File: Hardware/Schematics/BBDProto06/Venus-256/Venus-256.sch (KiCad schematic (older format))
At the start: 2 parts

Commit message: Added the hierarchical sheets
Added the hierarchical sheets for Cell Master and Slave
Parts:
- removed U? (x2): ATSAME70Q21A-AN, Package_QFP:LQFP-144_20x20mm_P0.5mm, symbol MCU_Microchip_SAME:ATSAME70Q21A-AN
- added C? (x14): 100nF, symbol Device:C_Small
- added C?: 10uF, symbol Device:C_Small
- added C?: 10pF, symbol Device:C_Small
- added D?: LED_ARGB, symbol Device:LED_ARGB
- added J406: ARM JTAG, symbol Connector_Generic:Conn_02x10_Odd_Even
- added J?: ADVREF, symbol Connector_Generic:Conn_01x01
- added L200: L, symbol Device:L
- added R400, R401, R402, R403: 0R, symbol Device:R_Small
- added R?: 5.62K, symbol Device:R_Small
- added U1: ATSAME70Q21A-AN, Package_QFP:LQFP-144_20x20mm_P0.5mm, symbol MCU_Microchip_SAME:ATSAME70Q21A-AN
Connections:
- net labels added: AFE0_AD0, AFE0_AD1, DAC0, DAC1, GND, SPI0_MISO, SPI0_MOSI, SPI0_SPCK, SPI1_MISO, SPI1_MOSI, SPI1_NPCS0, SPI1_NPCS1, SPI1_NPCS2, SPI1_NPCS3, SPI1_SPCK, SWCLK, SWDIO, TARGET_RESET, TRACESWO, USBD+, USBD-, VCC_3V3, VCC_MCU_P3V3, VDDCORE
- wire segments 0 -> 189
- no-connect marks 0 -> 8
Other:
- note added: "SWCLK"
- note added: "SWDIO"
- note added: "TARGET_RESET"
- note added: "TRACESWO"

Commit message: Updated the Cell Master and Slave schematics
Updated the Cell Master and Slave schematics
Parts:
- removed C? (x14): 100nF, symbol Device:C_Small
- removed C?: 10uF, symbol Device:C_Small
- removed C?: 10pF, symbol Device:C_Small
- removed D?: LED_ARGB, symbol Device:LED_ARGB
- removed J406: ARM JTAG, symbol Connector_Generic:Conn_02x10_Odd_Even
- removed J?: ADVREF, symbol Connector_Generic:Conn_01x01
- removed L200: L, symbol Device:L
- removed R400, R401, R402, R403: 0R, symbol Device:R_Small
- removed R?: 5.62K, symbol Device:R_Small
- removed U1: ATSAME70Q21A-AN, Package_QFP:LQFP-144_20x20mm_P0.5mm, symbol MCU_Microchip_SAME:ATSAME70Q21A-AN
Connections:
- net labels removed: AFE0_AD0, AFE0_AD1, DAC0, DAC1, GND, SPI0_MISO, SPI0_MOSI, SPI0_SPCK, SPI1_MISO, SPI1_MOSI, SPI1_NPCS0, SPI1_NPCS1, SPI1_NPCS2, SPI1_NPCS3, SPI1_SPCK, SWCLK, SWDIO, TARGET_RESET, TRACESWO, USBD+, USBD-, VCC_3V3, VCC_MCU_P3V3, VDDCORE
- wire segments 189 -> 0
- no-connect marks 8 -> 0
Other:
- note removed: "SWCLK"
- note removed: "SWDIO"
- note removed: "TARGET_RESET"
- note removed: "TRACESWO"

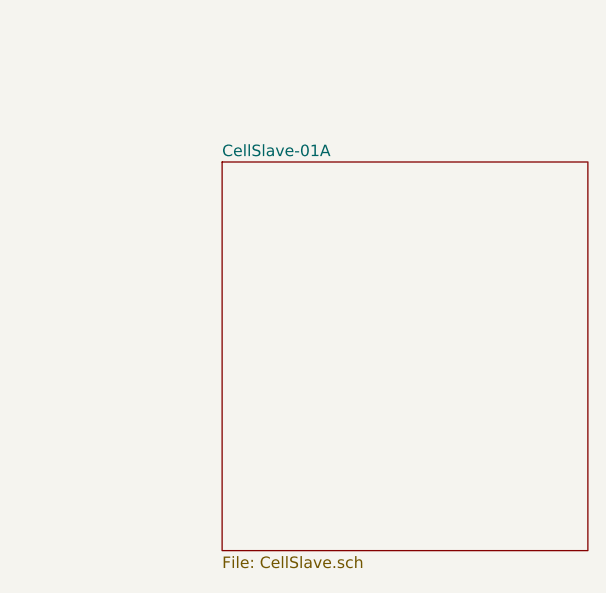
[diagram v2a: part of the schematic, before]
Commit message: Added Cell Slave capacitors
Added Cell Slave capacitors
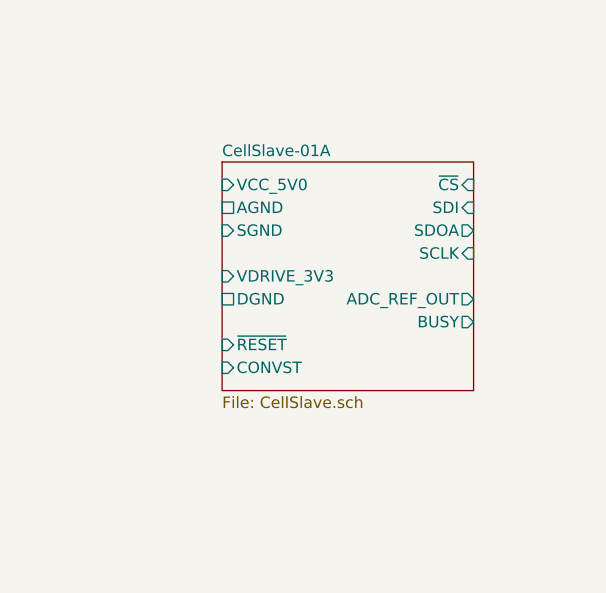
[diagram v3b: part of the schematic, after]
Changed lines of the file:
@@
 $EndSheet
 $Sheet
-S 5000 3500 1600 1700
+S 5000 3500 1100 1000
 U 5AE9ECEB
 F0 "CellSlave-01A" 50
 F1 "CellSlave.sch" 50
+F2 "DGND" U L 5000 4100 50
+F3 "BUSY" O R 6100 4200 50
+F4 "~CS" I R 6100 3600 50
+F5 "VDRIVE_3V3" I L 5000 4000 50
+F6 "SDI" I R 6100 3700 50
+F7 "SDOA" O R 6100 3800 50
+F8 "SCLK" I R 6100 3900 50
+F9 "AGND" U L 5000 3700 50
+F10 "VCC_5V0" I L 5000 3600 50
+F11 "SGND" I L 5000 3800 50
+F12 "ADC_REF_OUT" O R 6100 4100 50
+F13 "~RESET" I L 5000 4300 50
+F14 "CONVST" I L 5000 4400 50
 $EndSheet
 $EndSCHEMATC

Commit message: Completed the Cell Master and Slave schematics
Completed the Cell Master and Slave schematics
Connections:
- net labels added: GND
- wire segments 0 -> 148

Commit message: Added ADG715 switch array
Added ADG715 switch array
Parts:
- added U?: ADG715, Package_SO:TSSOP-24_4.4x7.8mm_P0.65mm, symbol Analog:ADG715
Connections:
- wire segments 148 -> 218

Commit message: Started to rearrange the Venus-256 PCB
Started to rearrange the Venus-256 PCB
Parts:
- gave numbers to parts that had none: 1
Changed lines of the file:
@@
 $Descr A4 11693 8268
 encoding utf-8
-Sheet 1 8
+Sheet 1 9
 Title "Venus-256"
 Date "2018-04-06"
@@
 $EndSheet
 $Comp
-L power:GND #PWR?
+L power:GND #PWR07
 U 1 1 5AE8F6FC
 P 4100 3300
-F 0 "#PWR?" H 4100 3050 50  0001 C CNN
+F 0 "#PWR07" H 4100 3050 50  0001 C CNN
 F 1 "GND" H 4105 3127 50  0000 C CNN
 F 2 "" H 4100 3300 50  0001 C CNN
@@
 	4100 3100 4100 3300
 $Comp
-L power:GND #PWR?
+L power:GND #PWR02
 U 1 1 5AE8F71C
 P 1000 3000
-F 0 "#PWR?" H 1000 2750 50  0001 C CNN
+F 0 "#PWR02" H 1000 2750 50  0001 C CNN
 F 1 "GND" H 1005 2827 50  0000 C CNN
 F 2 "" H 1000 3000 50  0001 C CNN
@@
 	1000 2800 1000 3000
 $Comp
-L power:GND #PWR?
+L power:GND #PWR01
 U 1 1 5AE8F730
 P 1000 1500
-F 0 "#PWR?" H 1000 1250 50  0001 C CNN
+F 0 "#PWR01" H 1000 1250 50  0001 C CNN
 F 1 "GND" H 1005 1327 50  0000 C CNN
 F 2 "" H 1000 1500 50  0001 C CNN
@@
 Connection ~ 800  1000
 $Comp
-L power:GND #PWR?
+L power:GND #PWR09
 U 1 1 5AE90A11
 P 9900 1600
-F 0 "#PWR?" H 9900 1350 50  0001 C CNN
+F 0 "#PWR09" H 9900 1350 50  0001 C CNN
 F 1 "GND" H 9905 1427 50  0000 C CNN
 F 2 "" H 9900 1600 50  0001 C CNN
@@
 	9900 1400 9900 1600
 $Comp
-L power:GND #PWR?
+L power:GND #PWR013
 U 1 1 5AE919C7
 P 10100 1600
-F 0 "#PWR?" H 10100 1350 50  0001 C CNN
+F 0 "#PWR013" H 10100 1350 50  0001 C CNN
 F 1 "GND" H 10105 1427 50  0000 C CNN
 F 2 "" H 10100 1600 50  0001 C CNN
@@
 	10400 2300 9800 2300
 $Comp
-L power:GND #PWR?
+L power:GND #PWR010
 U 1 1 5AE958F1
 P 9900 2900
-F 0 "#PWR?" H 9900 2650 50  0001 C CNN
+F 0 "#PWR010" H 9900 2650 50  0001 C CNN
 F 1 "GND" H 9905 2727 50  0000 C CNN
 F 2 "" H 9900 2900 50  0001 C CNN
@@
 	9900 2700 9900 2900
 $Comp
-L power:GND #PWR?
+L power:GND #PWR014
 U 1 1 5AE958F9
 P 10100 2900
-F 0 "#PWR?" H 10100 2650 50  0001 C CNN
+F 0 "#PWR014" H 10100 2650 50  0001 C CNN
 F 1 "GND" H 10105 2727 50  0000 C CNN
 F 2 "" H 10100 2900 50  0001 C CNN
@@
 	10400 3600 9800 3600
 $Comp
-L power:GND #PWR?
+L power:GND #PWR011
 U 1 1 5AE96319
 P 9900 4200
-F 0 "#PWR?" H 9900 3950 50  0001 C CNN
+F 0 "#PWR011" H 9900 3950 50  0001 C CNN
 F 1 "GND" H 9905 4027 50  0000 C CNN
 F 2 "" H 9900 4200 50  0001 C CNN
@@
 	9900 4000 9900 4200
 $Comp
-L power:GND #PWR?
+L power:GND #PWR015
 U 1 1 5AE96321
 P 10100 4200
-F 0 "#PWR?" H 10100 3950 50  0001 C CNN
+F 0 "#PWR015" H 10100 3950 50  0001 C CNN
 F 1 "GND" H 10105 4027 50  0000 C CNN
 F 2 "" H 10100 4200 50  0001 C CNN
@@
 	10400 4900 9800 4900
 $Comp
-L power:GND #PWR?
+L power:GND #PWR012
 U 1 1 5AE96EDB
 P 9900 5500
-F 0 "#PWR?" H 9900 5250 50  0001 C CNN
+F 0 "#PWR012" H 9900 5250 50  0001 C CNN
 F 1 "GND" H 9905 5327 50  0000 C CNN
 F 2 "" H 9900 5500 50  0001 C CNN
@@
 	9900 5300 9900 5500
 $Comp
-L power:GND #PWR?
+L power:GND #PWR016
 U 1 1 5AE96EE3
 P 10100 5500
-F 0 "#PWR?" H 10100 5250 50  0001 C CNN
+F 0 "#PWR016" H 10100 5250 50  0001 C CNN
 F 1 "GND" H 10105 5327 50  0000 C CNN
 F 2 "" H 10100 5500 50  0001 C CNN
@@
 	2800 1300 3500 1300
 $Comp
-L Analog:ADG715 U?
+L Analog:ADG715 U1
 U 1 1 5AE36C1A
 P 1800 4600
-F 0 "U?" H 1300 5200 50  0000 C CNN
+F 0 "U1" H 1300 5200 50  0000 C CNN
 F 1 "ADG715" H 1400 4100 50  0000 C CNN
 F 2 "Package_SO:TSSOP-24_4.4x7.8mm_P0.65mm" H 2800 4100 50  0001 C CIN
@@
 $EndComp
 $Comp
-L power:GND #PWR?
+L power:GND #PWR04
 U 1 1 5AE36CCF
 P 2000 5500
-F 0 "#PWR?" H 2000 5250 50  0001 C CNN
+F 0 "#PWR04" H 2000 5250 50  0001 C CNN
 F 1 "GND" H 2005 5327 50  0000 C CNN
 F 2 "" H 2000 5500 50  0001 C CNN
@@
 	2000 5200 2000 5500
 $Comp
-L power:GND #PWR?
+L power:GND #PWR03
 U 1 1 5AE90B6E
 P 1900 5300
-F 0 "#PWR?" H 1900 5050 50  0001 C CNN
+F 0 "#PWR03" H 1900 5050 50  0001 C CNN
 F 1 "GND" H 1905 5127 50  0000 C CNN
 F 2 "" H 1900 5300 50  0001 C CNN
@@
 	2300 3600 2300 3700
 $Comp
-L power:GND #PWR?
+L power:GND #PWR06
 U 1 1 5AEC21F3
 P 2300 3700
-F 0 "#PWR?" H 2300 3450 50  0001 C CNN
+F 0 "#PWR06" H 2300 3450 50  0001 C CNN
 F 1 "GND" H 2305 3527 50  0000 C CNN
 F 2 "" H 2300 3700 50  0001 C CNN
@@
 	2100 3200 2100 3300
 $Comp
-L power:GND #PWR?
+L power:GND #PWR05
 U 1 1 5AECD1C2
 P 2100 3300
-F 0 "#PWR?" H 2100 3050 50  0001 C CNN
+F 0 "#PWR05" H 2100 3050 50  0001 C CNN
 F 1 "GND" H 2105 3127 50  0000 C CNN
 F 2 "" H 2100 3300 50  0001 C CNN
@@
 $EndSheet
 $Comp
-L power:GND #PWR?
+L power:GND #PWR08
 U 1 1 5AF03082
 P 4100 6600
-F 0 "#PWR?" H 4100 6350 50  0001 C CNN
+F 0 "#PWR08" H 4100 6350 50  0001 C CNN
 F 1 "GND" H 4105 6427 50  0000 C CNN
 F 2 "" H 4100 6600 50  0001 C CNN

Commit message: Added a 5th cell-slave
Added a 5th cell-slave
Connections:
- wire segments 218 -> 242
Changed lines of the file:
@@
 EELAYER 26 0
 EELAYER END
-$Descr A4 11693 8268
+$Descr A3 16535 11693
 encoding utf-8
-Sheet 1 9
+Sheet 1 10
 Title "Venus-256"
 Date "2018-04-06"
@@
 	1500 3600 1700 3600
 $Sheet
-S 4200 4200 1300 2300
+S 4200 6550 1300 2300
 U 5AF0307C
 F0 "CellMaster-02" 50
 F1 "CellMaster.sch" 50
-F2 "VCC_MCU_P3V3" I L 4200 4300 50
-F3 "VDDCORE" I L 4200 4400 50
-F4 "GND" I L 4200 6400 50
-F5 "TRACESWO" O L 4200 4600 50
-F6 "SWDIO" B L 4200 4700 50
-F7 "SWCLK" I L 4200 4800 50
-F8 "TARGET_RESET" I L 4200 4900 50
-F9 "SPI1_NPCS0" O R 5500 4800 50
-F10 "SPI0_MISO" O L 4200 5100 50
-F11 "SPI0_MOSI" I L 4200 5200 50
-F12 "SPI0_SPCK" I L 4200 5300 50
-F13 "SPI1_NPCS2" O R 5500 5600 50
-F14 "SPI1_NPCS1" O R 5500 5200 50
-F15 "DAC0" O R 5500 4400 50
-F16 "SPI1_NPCS3" O R 5500 6000 50
-F17 "SPI1_MISO" I R 5500 6200 50
-F18 "SPI1_MOSI" O R 5500 6300 50
-F19 "SPI1_SPCK" O R 5500 6400 50
-F20 "ADC_CONVST0" O R 5500 4600 50
-F21 "ADC_BUSY0" I R 5500 4700 50
-F22 "ADC_BUSY1" I R 5500 5100 50
-F23 "ADC_BUSY2" I R 5500 5500 50
-F24 "ADC_BUSY3" I R 5500 5900 50
-F25 "ADC_CONVST1" O R 5500 5000 50
-F26 "ADC_CONVST2" O R 5500 5400 50
-F27 "ADC_CONVST3" O R 5500 5800 50
-F28 "ADC_RESET" I R 5500 4300 50
+F2 "VCC_MCU_P3V3" I L 4200 6650 50
+F3 "VDDCORE" I L 4200 6750 50
+F4 "GND" I L 4200 8750 50
+F5 "TRACESWO" O L 4200 6950 50
+F6 "SWDIO" B L 4200 7050 50
+F7 "SWCLK" I L 4200 7150 50
+F8 "TARGET_RESET" I L 4200 7250 50
+F9 "SPI1_NPCS0" O R 5500 7150 50
+F10 "SPI0_MISO" O L 4200 7450 50
+F11 "SPI0_MOSI" I L 4200 7550 50
+F12 "SPI0_SPCK" I L 4200 7650 50
+F13 "SPI1_NPCS2" O R 5500 7950 50
+F14 "SPI1_NPCS1" O R 5500 7550 50
+F15 "DAC0" O R 5500 6750 50
+F16 "SPI1_NPCS3" O R 5500 8350 50
+F17 "SPI1_MISO" I R 5500 8550 50
+F18 "SPI1_MOSI" O R 5500 8650 50
+F19 "SPI1_SPCK" O R 5500 8750 50
+F20 "ADC_CONVST0" O R 5500 6950 50
+F21 "ADC_BUSY0" I R 5500 7050 50
+F22 "ADC_BUSY1" I R 5500 7450 50
+F23 "ADC_BUSY2" I R 5500 7850 50
+F24 "ADC_BUSY3" I R 5500 8250 50
+F25 "ADC_CONVST1" O R 5500 7350 50
+F26 "ADC_CONVST2" O R 5500 7750 50
+F27 "ADC_CONVST3" O R 5500 8150 50
+F28 "ADC_RESET" I R 5500 6650 50
 $EndSheet
 $Comp
 L power:GND #PWR08
 U 1 1 5AF03082
-P 4100 6600
-F 0 "#PWR08" H 4100 6350 50  0001 C CNN
-F 1 "GND" H 4105 6427 50  0000 C CNN
-F 2 "" H 4100 6600 50  0001 C CNN
-F 3 "" H 4100 6600 50  0001 C CNN
-	1    4100 6600
+P 4100 8950
+F 0 "#PWR08" H 4100 8700 50  0001 C CNN
+F 1 "GND" H 4105 8777 50  0000 C CNN
+F 2 "" H 4100 8950 50  0001 C CNN
+F 3 "" H 4100 8950 50  0001 C CNN
+	1    4100 8950
 	1    0    0    -1
 $EndComp
 Wire Wire Line
-	4200 6400 4100 6400
-Wire Wire Line
-	4100 6400 4100 6600
-Wire Wire Line
-	4200 5100 3900 5100
-Wire Wire Line
-	4200 4400 4100 4400
-Wire Wire Line
-	4100 4400 4100 4300
-Wire Wire Line
-	4200 4300 4100 4300
-Connection ~ 4100 4300
-Wire Wire Line
-	2500 4300 4100 4300
-Wire Wire Line
-	3900 5100 3900 1800
+	4200 8750 4100 8750
+Wire Wire Line
+	4100 8750 4100 8950
+Wire Wire Line
+	4200 7450 3900 7450
+Wire Wire Line
+	4200 6750 4100 6750
+Wire Wire Line
+	4100 6750 4100 6650
+Wire Wire Line
+	4200 6650 4100 6650
+Wire Wire Line
+	3900 7450 3900 1800
 Connection ~ 3900 1800
 Wire Wire Line
 	3900 1800 2500 1800
 Wire Wire Line
-	3800 5200 3800 1900
-Wire Wire Line
-	3800 5200 4200 5200
+	3800 7550 3800 1900
+Wire Wire Line
+	3800 7550 4200 7550
 Connection ~ 3800 1900
 Wire Wire Line
 	3800 1900 2600 1900
 Wire Wire Line
-	3700 5300 3700 2000
-Wire Wire Line
-	3700 5300 4200 5300
+	3700 7650 3700 2000
+Wire Wire Line
+	3700 7650 4200 7650
 Connection ~ 3700 2000
 Wire Wire Line
 	3700 2000 2700 2000
 Wire Wire Line
-	4200 4600 3500 4600
-Wire Wire Line
-	3500 4600 3500 1300
+	4200 6950 3500 6950
+Wire Wire Line
+	3500 6950 3500 1300
 Connection ~ 3500 1300
 Wire Wire Line
 	3500 1300 4200 1300
 Wire Wire Line
-	4200 4700 3400 4700
-Wire Wire Line
-	3400 4700 3400 1400
+	4200 7050 3400 7050
+Wire Wire Line
+	3400 7050 3400 1400
 Connection ~ 3400 1400
 Wire Wire Line
 	3400 1400 4200 1400
 Wire Wire Line
-	4200 4800 3300 4800
-Wire Wire Line
-	3300 4800 3300 1500
+	4200 7150 3300 7150
+Wire Wire Line
+	3300 7150 3300 1500
 Connection ~ 3300 1500
 Wire Wire Line
 	3300 1500 4200 1500
 Wire Wire Line
-	4200 4900 3200 4900
-Wire Wire Line
-	3200 4900 3200 1600
+	4200 7250 3200 7250
+Wire Wire Line
+	3200 7250 3200 1600
 Connection ~ 3200 1600
 Wire Wire Line
 	3200 1600 4200 1600
+Wire Wire Line
+	2500 4300 3000 4300
+Wire Wire Line
+	3000 4300 3000 6650
+Wire Wire Line
+	3000 6650 4100 6650
+Connection ~ 4100 6650
+$Sheet
+S 8500 6550 1300 1100
+U 5AFE7089
+F0 "CellSlave-02A" 50
+F1 "CellSlave.sch" 50
+F2 "DGND" U R 9800 7050 50
+F3 "BUSY" O L 8500 7050 50
+F4 "~CS" I L 8500 7150 50
+F5 "VDRIVE_3V3" I R 9800 6950 50
+F6 "SDI" I L 8500 7450 50
+F7 "SDOA" O L 8500 7350 50
+F8 "SCLK" I L 8500 7550 50
+F9 "AGND" U R 9800 6750 50
+F10 "VCC_5V0" I R 9800 6650 50
+F11 "SGND" I L 8500 6750 50
+F12 "~RESET" I L 8500 6650 50
+F13 "CONVST" I L 8500 6950 50
+$EndSheet
+Wire Wire Line
+	5500 6650 8500 6650
+Wire Wire Line
+	10300 5200 10300 6950
+Connection ~ 10300 5200
+Wire Wire Line
+	9800 6650 10400 6650
+Wire Wire Line
+	10400 6650 10400 4900
+Connection ~ 10400 4900
+Wire Wire Line
+	5500 6750 8500 6750
+Wire Wire Line
+	5500 6950 8500 6950
+Wire Wire Line
+	5500 7050 8500 7050
+Wire Wire Line
+	5500 7150 8500 7150
+Wire Wire Line
+	5500 8550 7800 8550
+Wire Wire Line
+	7800 8550 7800 7350
+Wire Wire Line
+	7800 7350 8500 7350
+Wire Wire Line
+	8500 7450 7900 7450
+Wire Wire Line
+	7900 7450 7900 8650
+Wire Wire Line
+	7900 8650 5500 8650
+Wire Wire Line
+	5500 8750 8000 8750
+Wire Wire Line
+	8000 8750 8000 7550
+Wire Wire Line
+	8000 7550 8500 7550
+$Comp
+L power:GND #PWR0101
+U 1 1 5B09A94C
+P 9900 7250
+F 0 "#PWR0101" H 9900 7000 50  0001 C CNN
+F 1 "GND" H 9905 7077 50  0000 C CNN
+F 2 "" H 9900 7250 50  0001 C CNN
+F 3 "" H 9900 7250 50  0001 C CNN
+	1    9900 7250
+	-1   0    0    -1
+$EndComp
+Wire Wire Line
+	9800 7050 9900 7050
+Wire Wire Line
+	9900 7050 9900 7250
+$Comp
+L power:GND #PWR0102
+U 1 1 5B09A954
+P 10100 7250
+F 0 "#PWR0102" H 10100 7000 50  0001 C CNN
+F 1 "GND" H 10105 7077 50  0000 C CNN
+F 2 "" H 10100 7250 50  0001 C CNN
+F 3 "" H 10100 7250 50  0001 C CNN
+	1    10100 7250
+	-1   0    0    -1
+$EndComp
+Wire Wire Line
+	10100 6750 10100 7250
+Wire Wire Line
+	9800 6750 10100 6750
+Wire Wire Line
+	9800 6950 10300 6950
 $EndSCHEMATC
